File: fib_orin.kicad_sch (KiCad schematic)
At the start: 1 part, among them J1201 Orin Nano

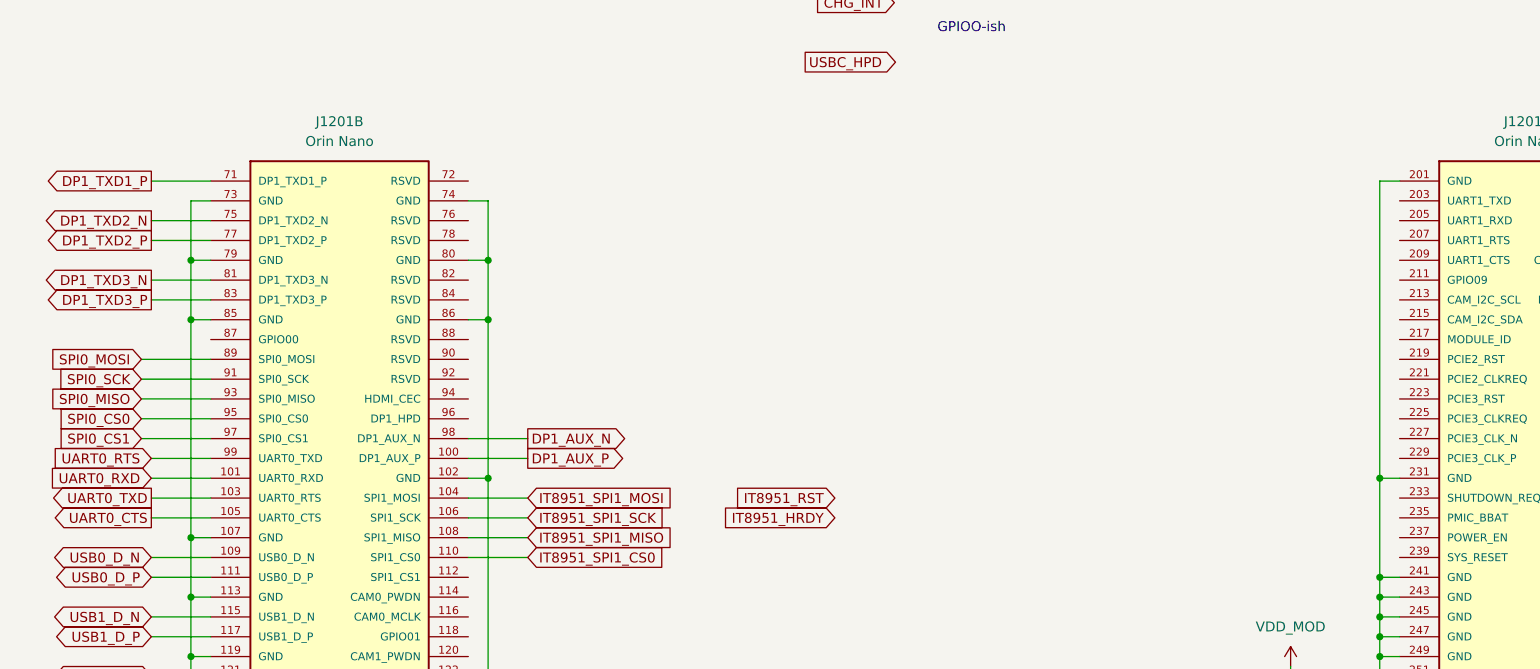
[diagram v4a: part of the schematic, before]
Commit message: refactored PCIe pages
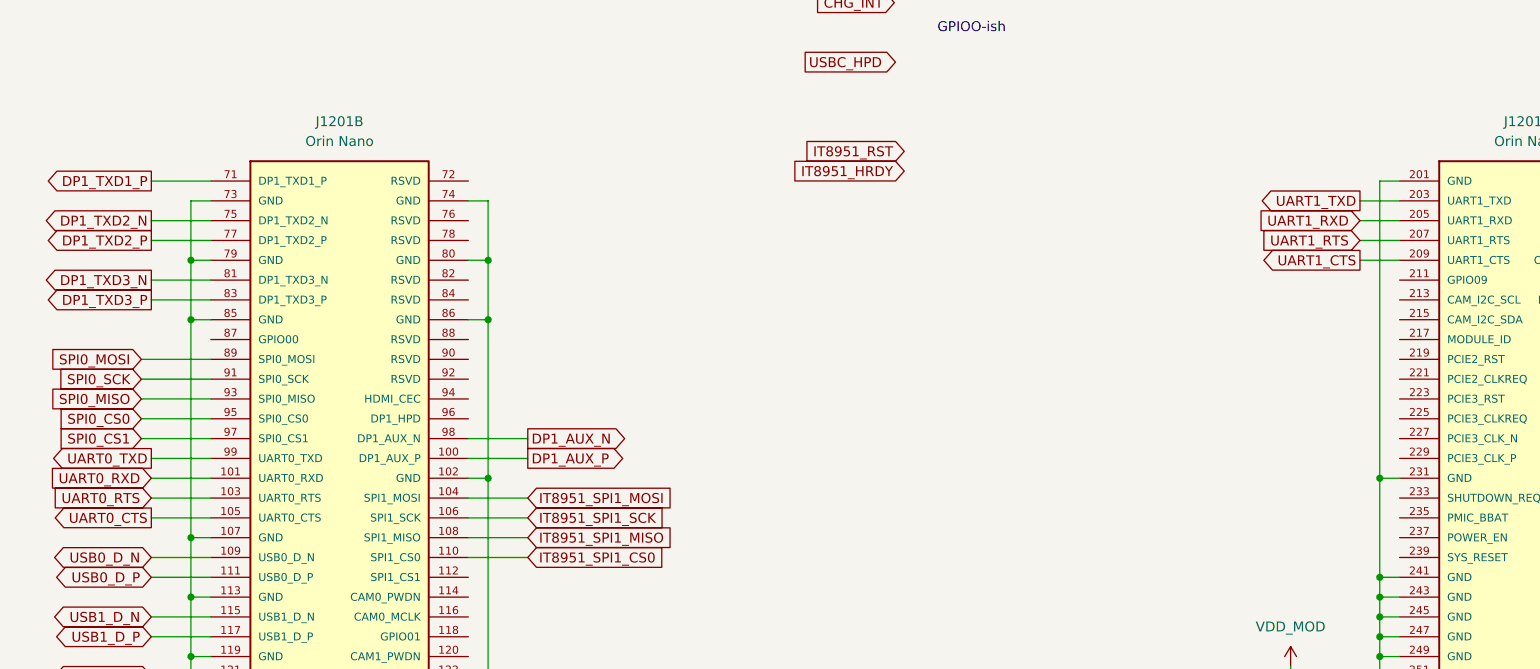
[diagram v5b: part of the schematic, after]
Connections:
- net UART0_RTS: now also J1201.103 (UART0_RTS); no longer J1201.99 (UART0_TXD)
- net UART0_TXD: now also J1201.99 (UART0_TXD); no longer J1201.103 (UART0_RTS)
- net UART1_TXD: now reaches J1201.203 (UART1_TXD)
- net UART1_RXD: now reaches J1201.205 (UART1_RXD)
- net UART1_RTS: now reaches J1201.207 (UART1_RTS)
- net UART1_CTS: now reaches J1201.209 (UART1_CTS)
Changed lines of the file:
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@@
 	(wire
 		(pts
+			(xy 262.89 177.8) (xy 267.97 177.8)
+		)
+		(stroke
+			(width 0)
+			(type default)
+		)
+	)
+	(wire
+		(pts
 			(xy 265.43 228.6) (xy 265.43 247.65)
 		)
@@
 	(wire
 		(pts
+			(xy 262.89 175.26) (xy 267.97 175.26)
+		)
+		(stroke
+			(width 0)
+			(type default)
+		)
+	)
+	(wire
+		(pts
 			(xy 307.34 60.96) (xy 300.99 60.96)
 		)
@@
 	(wire
 		(pts
+			(xy 262.89 170.18) (xy 267.97 170.18)
+		)
+		(stroke
+			(width 0)
+			(type default)
+		)
+	)
+	(wire
+		(pts
 			(xy 148.59 71.12) (xy 151.13 71.12)
 		)
@@
 	(wire
 		(pts
+			(xy 262.89 172.72) (xy 267.97 172.72)
+		)
+		(stroke
+			(width 0)
+			(type default)
+		)
+	)
+	(wire
+		(pts
 			(xy 303.53 132.08) (xy 303.53 124.46)
 		)
@@
 		)
 	)
-	(global_label "UART0_RXD"
-		(shape input)
-		(at 107.95 205.74 180)
+	(global_label "USBSS0_TX_P"
+		(shape output)
+		(at 307.34 83.82 0)
 		(effects
 			(font
 				(size 1.27 1.27)
 			)
-			(justify right)
+			(justify left)
 		)
 		(property "Intersheetrefs" "${INTERSHEET_REFS}"
-			(at 93.98 205.74 0)
+			(at 323.215 83.82 0)
 			(effects
 				(font
-					(size 1.27 1.27)
+					(size 1.1 1.1)
 				)
-				(justify right)
+				(justify left)
 				(hide yes)
 			)
 		)
 	)
-	(global_label "USBSS0_TX_P"
-		(shape output)
-		(at 307.34 83.82 0)
+	(global_label "UART1_RTS"
+		(shape input)
+		(at 262.89 175.26 180)
 		(effects
 			(font
 				(size 1.27 1.27)
 			)
-			(justify left)
+			(justify right)
 		)
 		(property "Intersheetrefs" "${INTERSHEET_REFS}"
-			(at 323.215 83.82 0)
+			(at 248.92 175.26 0)
 			(effects
 				(font
-					(size 1.1 1.1)
+					(size 1.27 1.27)
 				)
-				(justify left)
+				(justify right)
 				(hide yes)
 			)
@@
 	(global_label "IT8951_RST"
 		(shape input)
-		(at 195.58 208.28 180)
+		(at 204.47 163.83 180)
 		(fields_autoplaced yes)
 		(effects
@@
 		)
 		(property "Intersheetrefs" "${INTERSHEET_REFS}"
-			(at 181.7697 208.28 0)
+			(at 190.6597 163.83 0)
 			(effects
 				(font
@@
 		)
 	)
-	(global_label "UART0_CTS"
-		(shape output)
-		(at 107.95 210.82 180)
+	(global_label "PCIE1_RX0_P"
+		(shape input)
+		(at 261.62 86.36 180)
 		(effects
 			(font
@@
 		)
 		(property "Intersheetrefs" "${INTERSHEET_REFS}"
-			(at 93.98 210.82 0)
+			(at 240.665 86.36 0)
 			(effects
 				(font
 					(size 1.27 1.27)
 				)
-				(justify right)
+				(justify left)
 				(hide yes)
 			)
 		)
 	)
-	(global_label "PCIE1_RX0_P"
+	(global_label "SPI0_SCK"
 		(shape input)
-		(at 261.62 86.36 180)
+		(at 106.68 193.04 180)
+		(fields_autoplaced yes)
 		(effects
 			(font
@@
 		)
 		(property "Intersheetrefs" "${INTERSHEET_REFS}"
-			(at 240.665 86.36 0)
+			(at 94.6839 193.04 0)
 			(effects
 				(font
 					(size 1.27 1.27)
 				)
-				(justify left)
+				(justify right)
 				(hide yes)
 			)
 		)
 	)
-	(global_label "SPI0_SCK"
-		(shape input)
-		(at 106.68 193.04 180)
-		(fields_autoplaced yes)
+	(global_label "UART1_CTS"
+		(shape output)
+		(at 262.89 177.8 180)
 		(effects
 			(font
@@
 		)
 		(property "Intersheetrefs" "${INTERSHEET_REFS}"
-			(at 94.6839 193.04 0)
+			(at 248.92 177.8 0)
+			(effects
+				(font
+					(size 1.27 1.27)
+				)
+				(justify right)
+				(hide yes)
+			)
+		)
+	)
+	(global_label "UART0_TXD"
+		(shape output)
+		(at 107.95 203.2 180)
+		(effects
+			(font
+				(size 1.27 1.27)
+			)
+			(justify right)
+		)
+		(property "Intersheetrefs" "${INTERSHEET_REFS}"
+			(at 93.98 203.2 0)
 			(effects
 				(font
@@
 		)
 	)
+	(global_label "UART0_CTS"
+		(shape output)
+		(at 107.95 210.82 180)
+		(effects
+			(font
+				(size 1.27 1.27)
+			)
+			(justify right)
+		)
+		(property "Intersheetrefs" "${INTERSHEET_REFS}"
+			(at 93.98 210.82 0)
+			(effects
+				(font
+					(size 1.27 1.27)
+				)
+				(justify right)
+				(hide yes)
+			)
+		)
+	)
 	(global_label "SPI0_MOSI"
 		(shape input)
@@
 		)
 	)
+	(global_label "UART1_TXD"
+		(shape output)
+		(at 262.89 170.18 180)
+		(effects
+			(font
+				(size 1.27 1.27)
+			)
+			(justify right)
+		)
+		(property "Intersheetrefs" "${INTERSHEET_REFS}"
+			(at 248.92 170.18 0)
+			(effects
+				(font
+					(size 1.27 1.27)
+				)
+				(justify right)
+				(hide yes)
+			)
+		)
+	)
 	(global_label "DP1_TXD2_N"
 		(shape output)
@@
 		)
 	)
+	(global_label "UART1_RXD"
+		(shape input)
+		(at 262.89 172.72 180)
+		(effects
+			(font
+				(size 1.27 1.27)
+			)
+			(justify right)
+		)
+		(property "Intersheetrefs" "${INTERSHEET_REFS}"
+			(at 248.92 172.72 0)
+			(effects
+				(font
+					(size 1.27 1.27)
+				)
+				(justify right)
+				(hide yes)
+			)
+		)
+	)
 	(global_label "IT8951_SPI1_MOSI"
 		(shape input)
@@
 	(global_label "IT8951_HRDY"
 		(shape input)
-		(at 195.58 210.82 180)
+		(at 204.47 166.37 180)
 		(fields_autoplaced yes)
 		(effects
@@
 		)
 		(property "Intersheetrefs" "${INTERSHEET_REFS}"
-			(at 180.2577 210.82 0)
+			(at 189.1477 166.37 0)
 			(effects
 				(font
@@
 		)
 	)
+	(global_label "UART0_RTS"
+		(shape input)
+		(at 107.95 208.28 180)
+		(effects
+			(font
+				(size 1.27 1.27)
+			)
+			(justify right)
+		)
+		(property "Intersheetrefs" "${INTERSHEET_REFS}"
+			(at 93.98 208.28 0)
+			(effects
+				(font
+					(size 1.27 1.27)
+				)
+				(justify right)
+				(hide yes)
+			)
+		)
+	)
 	(global_label "PCIE0_CLKREQ*"
 		(shape output)
@@
 		)
 	)
+	(global_label "UART0_RXD"
+		(shape input)
+		(at 107.95 205.74 180)
+		(effects
+			(font
+				(size 1.27 1.27)
+			)
+			(justify right)
+		)
+		(property "Intersheetrefs" "${INTERSHEET_REFS}"
+			(at 93.98 205.74 0)
+			(effects
+				(font
+					(size 1.27 1.27)
+				)
+				(justify right)
+				(hide yes)
+			)
+		)
+	)
 	(global_label "PCIE1_TX0_P"
 		(shape output)
@@
 		)
 	)
-	(global_label "UART0_TXD"
-		(shape output)
-		(at 107.95 208.28 180)
-		(effects
-			(font
-				(size 1.27 1.27)
-			)
-			(justify right)
-		)
-		(property "Intersheetrefs" "${INTERSHEET_REFS}"
-			(at 93.98 208.28 0)
-			(effects
-				(font
-					(size 1.27 1.27)
-				)
-				(justify right)
-				(hide yes)
-			)
-		)
-	)
 	(global_label "DP1_TXD3_P"
 		(shape output)
@@
 			(effects
 				(font
-					(size 1.27 1.27)
-				)
-				(justify right)
-				(hide yes)
-			)
-		)
-	)
-	(global_label "UART0_RTS"
-		(shape input)
-		(at 107.95 203.2 180)
-		(effects
-			(font
-				(size 1.27 1.27)
-			)
-			(justify right)
-		)
-		(property "Intersheetrefs" "${INTERSHEET_REFS}"
-			(at 93.98 203.2 0)
-			(effects
-				(font

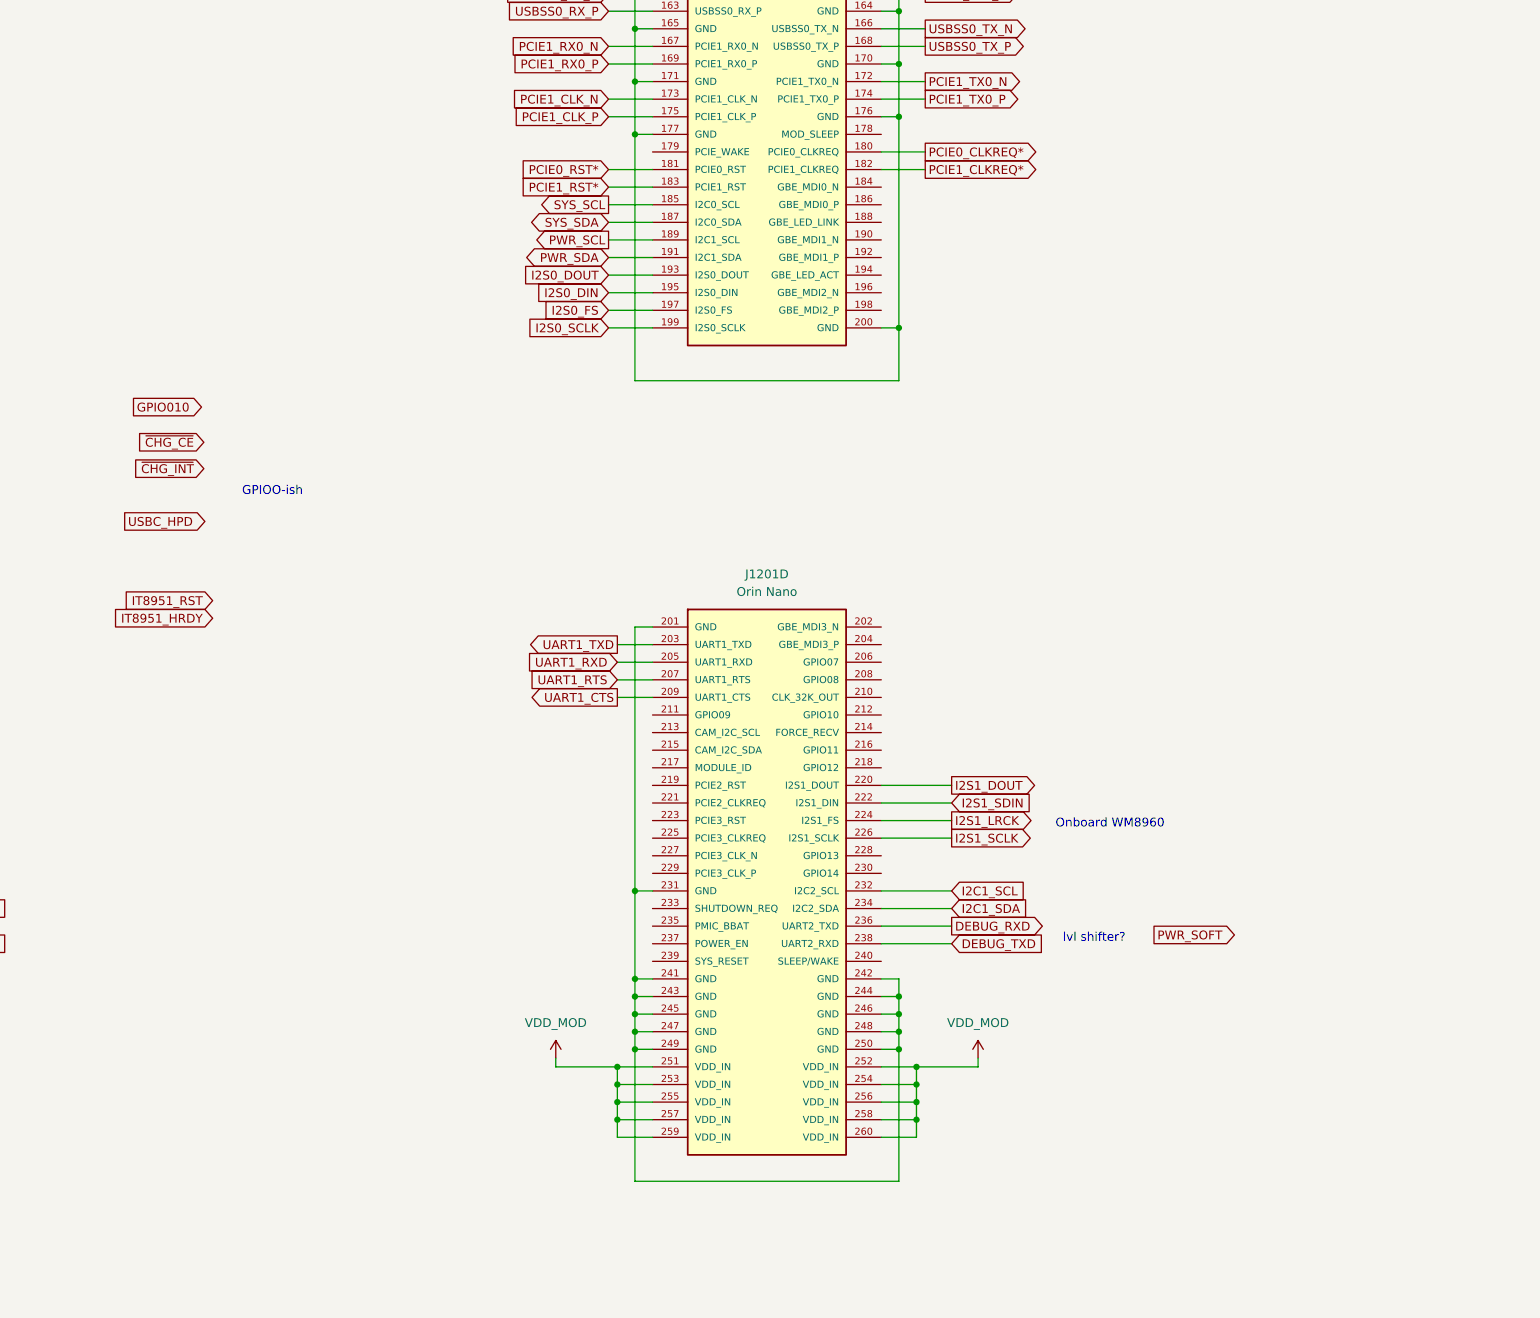
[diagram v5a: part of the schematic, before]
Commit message: added some missing footprints, stared working ono power-on and sequencing
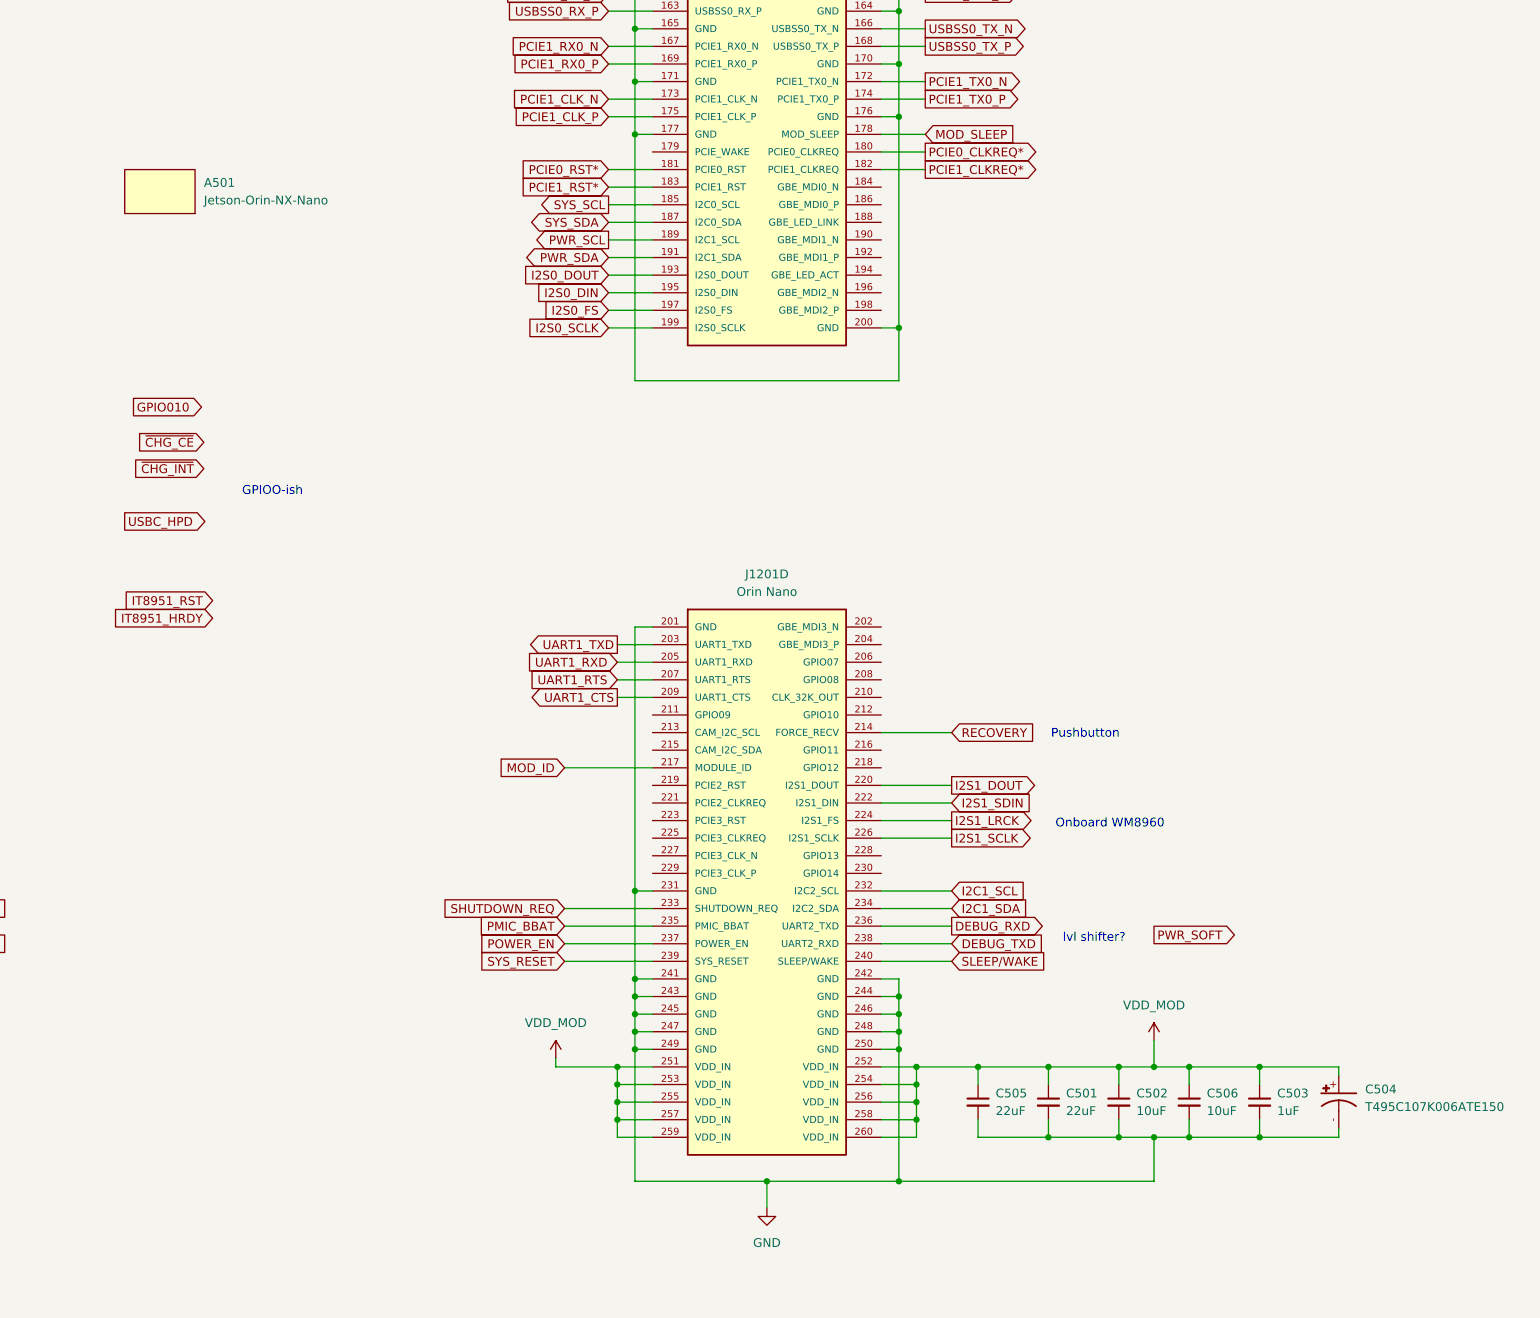
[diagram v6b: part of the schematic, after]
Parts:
- added A501: Jetson-Orin-NX-Nano, Fibel2:jetson-orin-nx-nano-module, symbol Fibel2:Jetson-Orin-NX-Nano
- added C501, C505: 22uF, Capacitor_SMD:C_0805_2012Metric, symbol Device:C_Small
- added C502, C506: 10uF, Capacitor_SMD:C_0603_1608Metric, symbol Device:C_Small
- added C503: 1uF, Capacitor_SMD:C_0603_1608Metric, symbol Device:C_Small
- added C504: T495C107K006ATE150, Fibel2:CAPMP6032X250, symbol Fibel2:T495C107K006ATE150
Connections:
- net VDD_MOD: now also C501.1, C502.1, C503.1, C504.+, C505.1, C506.1
- net GND: now reaches J1201.201 (GND), J1201.231 (GND), J1201.241 (GND), J1201.242 (GND), J1201.243 (GND), J1201.244 (GND), J1201.245 (GND), J1201.246 (GND), J1201.247 (GND), J1201.248 (GND), J1201.249 (GND), J1201.250 (GND)
- net GND: now also C501.2, C502.2, C503.2, C504.-, C505.2, C506.2
- net RECOVERY: now reaches J1201.214 (FORCE_RECV)
- net MOD_ID: now reaches J1201.217 (MODULE_ID)
- net SHUTDOWN_REQ: now reaches J1201.233 (SHUTDOWN_REQ)
- net PMIC_BBAT: now reaches J1201.235 (PMIC_BBAT)
- net POWER_EN: now reaches J1201.237 (POWER_EN)
- net SYS_RESET: now reaches J1201.239 (SYS_RESET)
- net SLEEP/WAKE: now reaches J1201.240 (SLEEP/WAKE)
- net MOD_SLEEP: now reaches J1201.178 (MOD_SLEEP)
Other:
- note added: "Pushbutton"
